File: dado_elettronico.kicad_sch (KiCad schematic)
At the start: 25 parts, among them Q1 2N2219, U1 NE555P, U2 4017

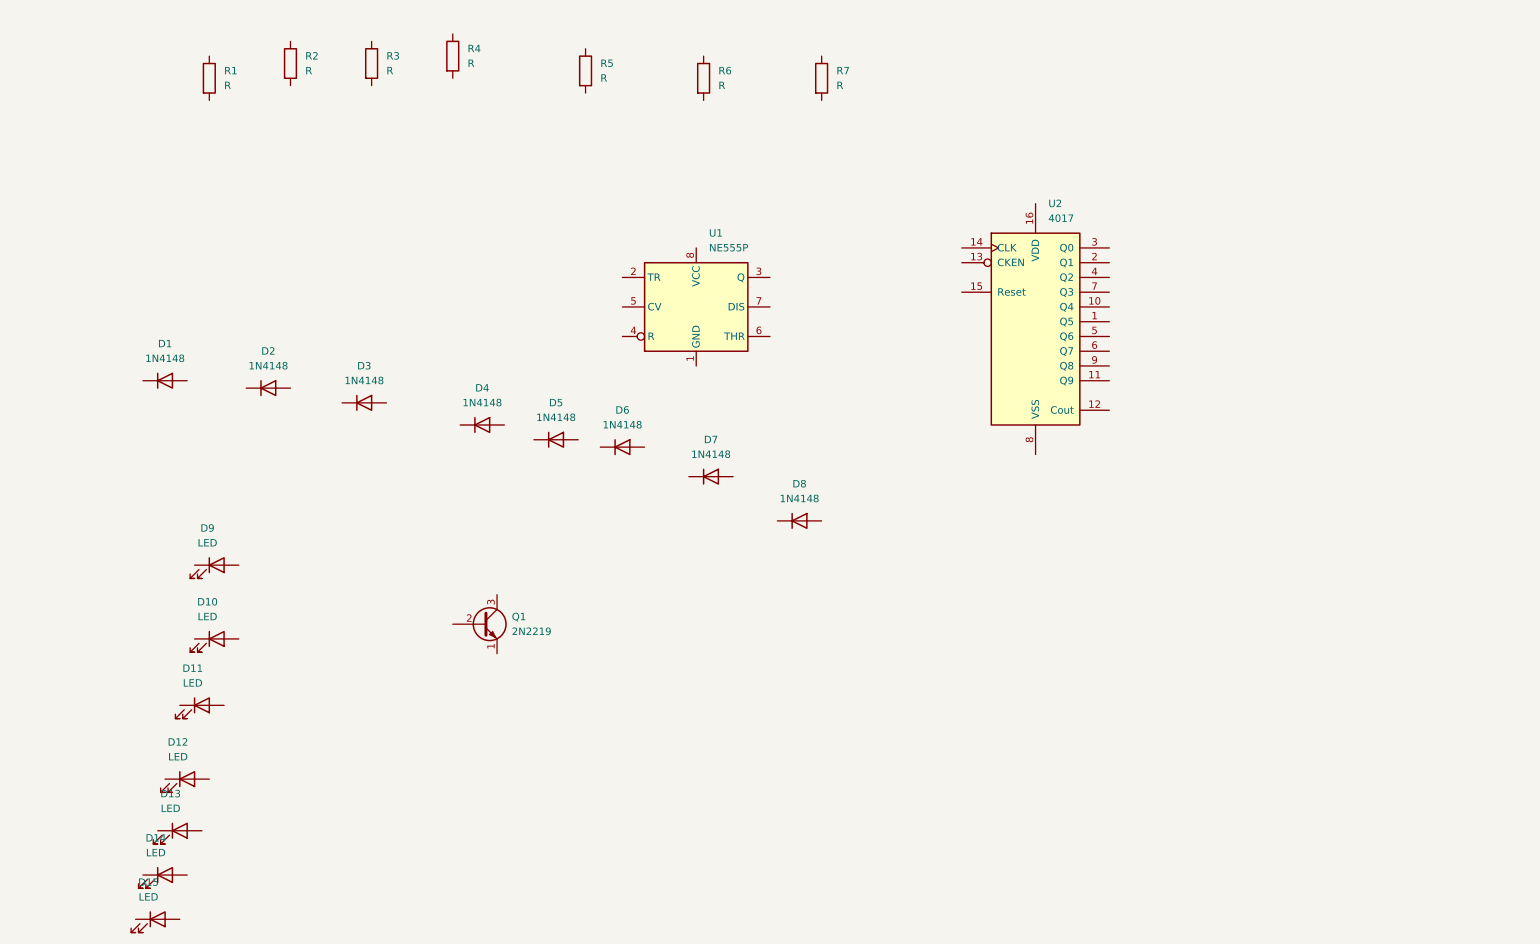
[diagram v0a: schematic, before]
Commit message: collegamento del contatore con i diodi
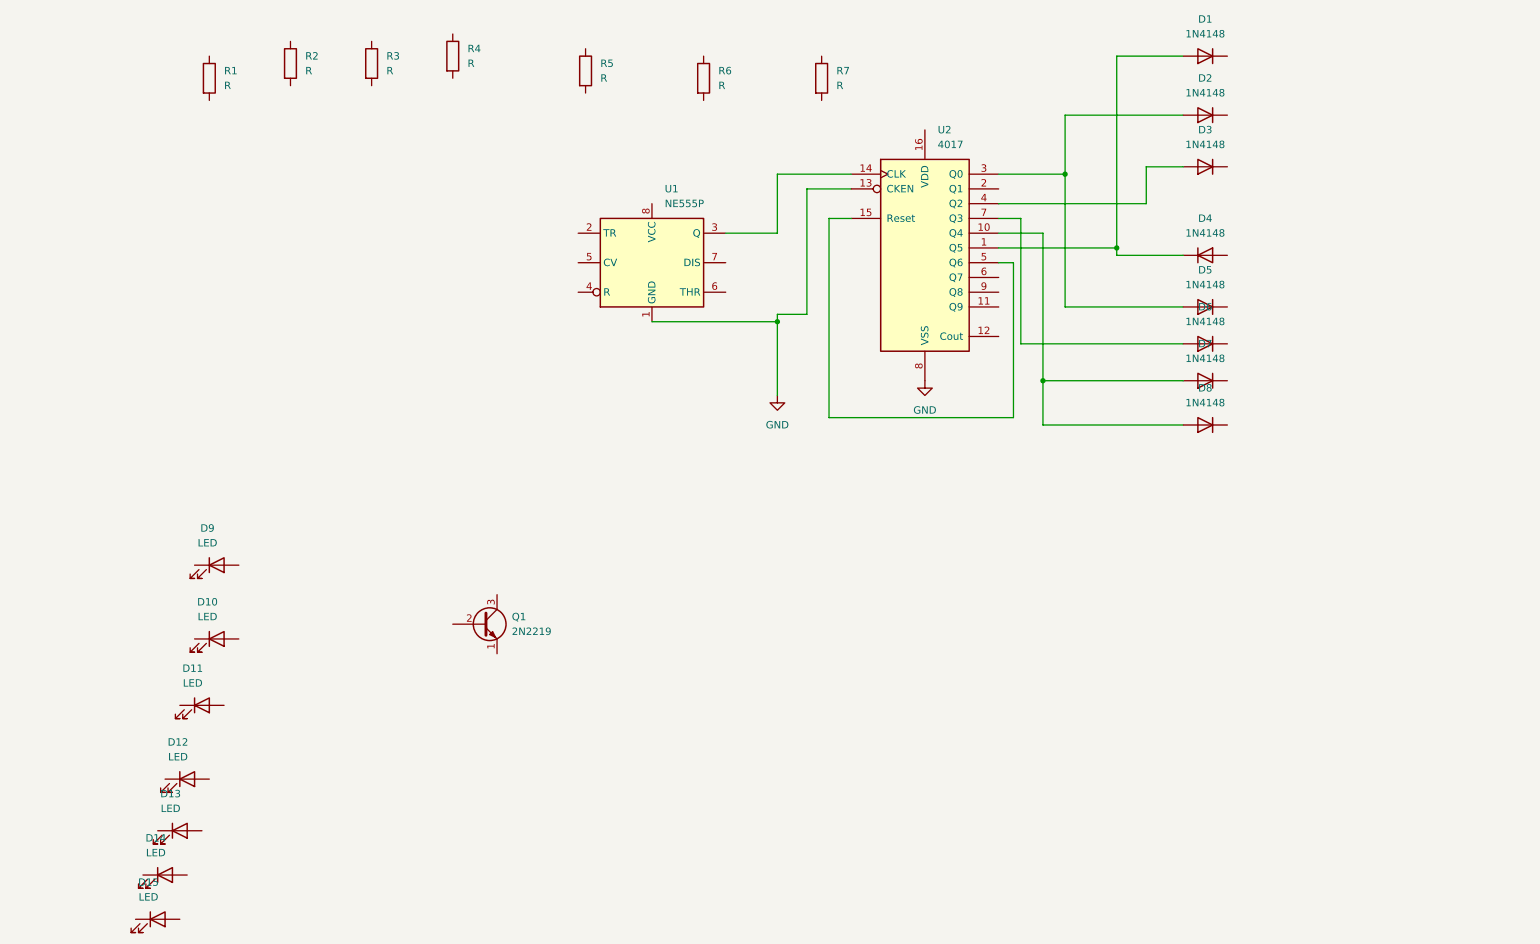
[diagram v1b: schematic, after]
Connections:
- net GND: now reaches U1.1 (GND)
- net GND: now also U2.13 (CKEN), U2.8 (VSS)
- net at U1.3 (Q): now also U2.14 (CLK)
- net at D2.2 (A): now also D5.2 (A), U2.3 (Q0)
- net at D7.2 (A): now also D8.2 (A), U2.10 (Q4)
- net at D1.2 (A): now also D4.1 (K), U2.1 (Q5)
- net at U2.15 (Reset): now also U2.5 (Q6)
- net at U2.4 (Q2): now also D3.2 (A)
- net at U2.7 (Q3): now also D6.2 (A)
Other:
- moved on the sheet: D1, D2, D3, D4, D5, D6, D7, D8, U1, U2

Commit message: schema elettrico completo
schema elettrico completo senza impronta componenti
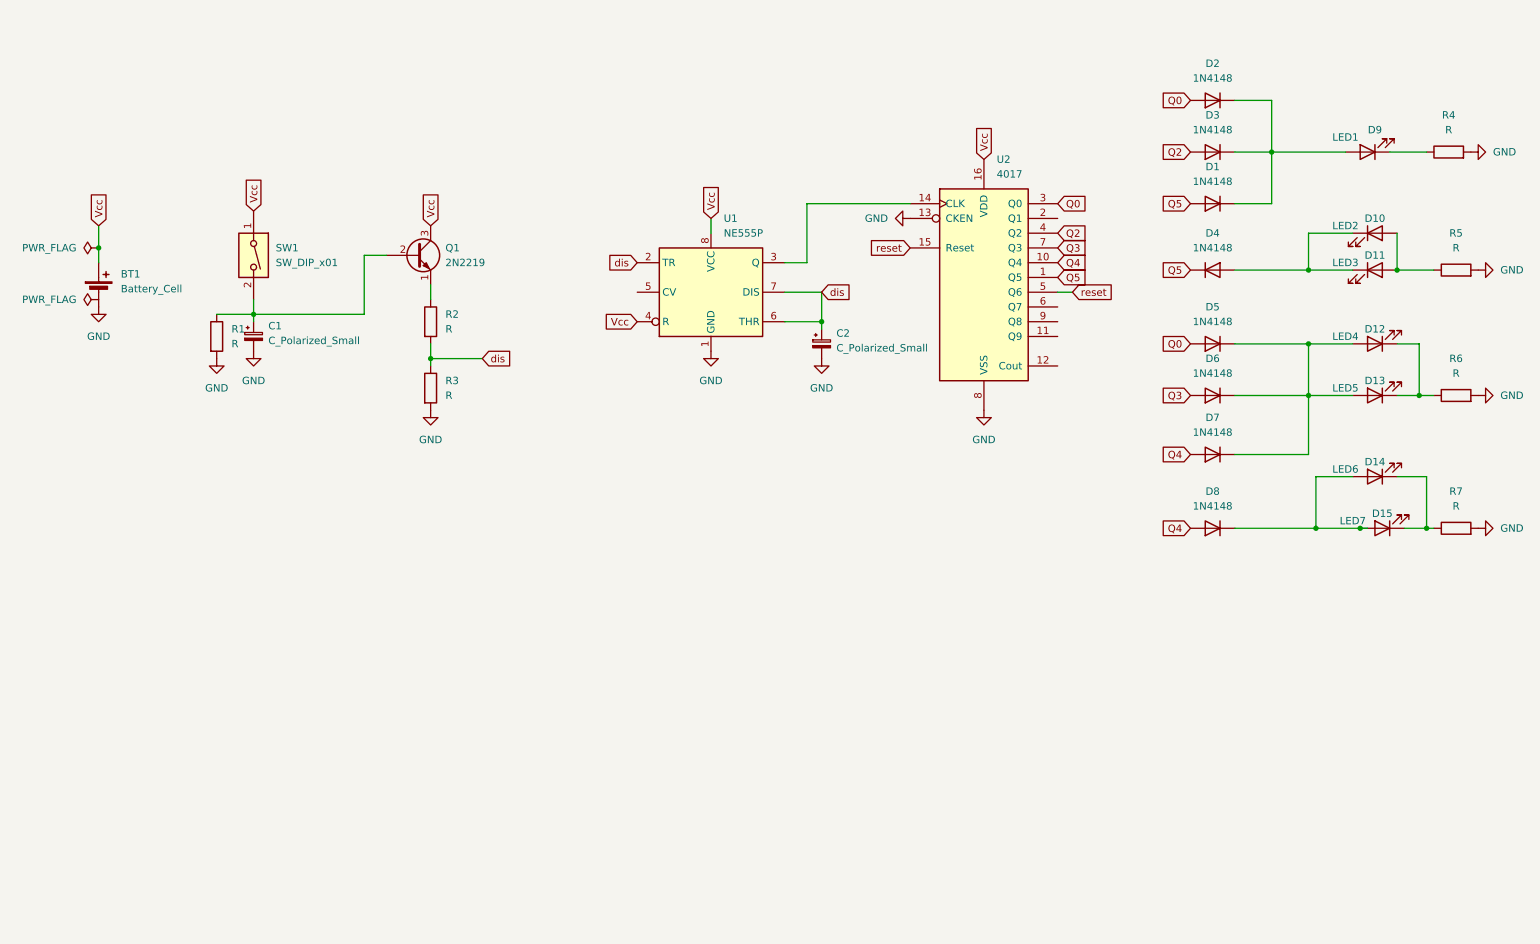
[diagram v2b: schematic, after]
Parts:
- added BT1: Battery_Cell, Battery:BatteryHolder_Keystone_1057_1x2032, symbol Device:Battery_Cell
- added C1, C2: C_Polarized_Small, symbol Device:C_Polarized_Small
- added SW1: SW_DIP_x01, symbol Switch:SW_DIP_x01
- D10: value LED -> LED2
- D11: value LED -> LED3
- D12: value LED -> LED4
- D13: value LED -> LED5
- D14: value LED -> LED6
- D15: value LED -> LED7
- D9: value LED -> LED1
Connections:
- net GND: now also R1.2, R3.2, R4.2, R5.2, R6.2, R7.2, BT1.2 (-), C1.2, C2.2
- net at R6.1: now also D12.1 (K), D13.1 (K)
- net at D15.1 (K): now also D14.1 (K), R7.1
- net at D15.2 (A): now also D14.2 (A), D8.1 (K)
- net at D9.1 (K): now also R4.1
- net at D9.2 (A): now also D1.1 (K), D2.1 (K), D3.1 (K)
- net dis: now reaches U1.2 (TR)
- net dis: now also R2.2, R3.1, U1.6 (THR), U1.7 (DIS), C2.1
- net Vcc: now reaches U1.4 (R)
- net Vcc: now also Q1.3 (C), U1.8 (VCC), U2.16 (VDD), BT1.1 (+), SW1.1
- net Q0: now reaches D2.2 (A), D5.2 (A), U2.3 (Q0)
- net at D7.1 (K): now also D12.2 (A), D13.2 (A), D5.1 (K), D6.1 (K)
- net Q4: now reaches D7.2 (A), D8.2 (A), U2.10 (Q4)
- net at R5.1: now also D10.2 (A), D11.2 (A)
- net Q5: now reaches D1.2 (A), D4.1 (K), U2.1 (Q5)
- net reset: now reaches U2.15 (Reset), U2.5 (Q6)
- net Q2: now reaches D3.2 (A), U2.4 (Q2)
- net Q3: now reaches D6.2 (A), U2.7 (Q3)
- net at D4.2 (A): now also D10.1 (K), D11.1 (K)
- net at R1.1: now also Q1.2 (B), C1.1, SW1.2
- net at Q1.1 (E): now also R2.1
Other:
- company: (none) -> Andrea
- title: (none) -> Dado Elettronico
- moved on the sheet: D1, D2, D3, D4, D5, D6, D7, D8, Q1, R1, R2, R3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
